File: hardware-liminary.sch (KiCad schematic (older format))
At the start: 2 parts, among them J1 Conn_01x05, J2 Conn_01x05

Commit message: Agregado modulo HLW8032
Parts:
- removed J1, J2: Conn_01x05, Connector_PinHeader_2.54mm:PinHeader_1x05_P2.54mm_Vertical, symbol Connector_Generic:Conn_01x05
- added JB1, JB2, JT1, JT2: Conn_01x03, Connector_PinHeader_2.54mm:PinHeader_1x03_P2.54mm_Vertical, symbol Connector_Generic:Conn_01x03
- added JB3, JT3: Conn_01x05, Connector_PinHeader_2.54mm:PinHeader_1x05_P2.54mm_Vertical, symbol Connector_Generic:Conn_01x05
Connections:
- net Bottom Board/3.3v: now also JB2.1 (Pin_1)
- net Bottom Board/GND: now also JB1.3 (Pin_3)
- net Bottom Board/OpenC: now also JB1.1 (Pin_1)
- net Bottom Board/PIR: now also JB2.3 (Pin_3)
- net Bottom Board/Relay: now also JB3.1 (Pin_1)
- net Top Board/3.3v: now also JT2.1 (Pin_1)
- net Top Board/GND: now also JT1.3 (Pin_3)
- net Top Board/OpenC: now also JT1.1 (Pin_1)
- net Top Board/PIR: now also JT2.3 (Pin_3)
- net Top Board/Relay: now also JT3.1 (Pin_1)
- new net Bottom Board/Enery_Pulses: JB3.5 (Pin_5)
- new net Bottom Board/Enery_Tx: JB3.3 (Pin_3)
- new net Top Board/Enery_Pulses: JT3.5 (Pin_5)
- new net Top Board/Enery_Tx: JT3.3 (Pin_3)
- no-connect marks 0 -> 8
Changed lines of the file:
@@
 $EndDescr
 $Sheet
-S 5550 3150 900  950
+S 5250 3000 900  1300
 U 5F84ED08
 F0 "Top Board" 50
 F1 "top_board.sch" 50
-F2 "3.3v" I L 5550 3300 50
-F3 "GND" U L 5550 3450 50
-F4 "OpenC" O L 5550 3750 50
-F5 "PIR" I L 5550 3600 50
-F6 "Relay" O L 5550 3900 50
+F2 "3.3v" I L 5250 3450 50
+F3 "GND" U L 5250 3300 50
+F4 "OpenC" O L 5250 3150 50
+F5 "PIR" I L 5250 3600 50
+F6 "Relay" O L 5250 3750 50
+F7 "Enery_Tx" I L 5250 3900 50
+F8 "Enery_Pulses" I L 5250 4050 50
 $EndSheet
 $Sheet
-S 2350 3150 1000 950
+S 2200 3000 1000 1300
 U 5F91F411
 F0 "Bottom Board" 50
 F1 "bottom_board.sch" 50
-F2 "3.3v" O R 3350 3300 50
-F3 "GND" U R 3350 3450 50
-F4 "OpenC" I R 3350 3750 50
-F5 "PIR" O R 3350 3600 50
-F6 "Relay" I R 3350 3900 50
+F2 "3.3v" O R 3200 3450 50
+F3 "GND" U R 3200 3300 50
+F4 "OpenC" I R 3200 3150 50
+F5 "PIR" O R 3200 3600 50
+F6 "Relay" I R 3200 3750 50
+F7 "Enery_Tx" O R 3200 3900 50
+F8 "Enery_Pulses" O R 3200 4050 50
 $EndSheet
 $Comp
-L Connector_Generic:Conn_01x05 J1
-U 1 1 5F94C7D4
-P 3850 3600
-F 0 "J1" H 3930 3642 50  0000 L CNN
-F 1 "Conn_01x05" H 3930 3551 50  0000 L CNN
-F 2 "Connector_PinHeader_2.54mm:PinHeader_1x05_P2.54mm_Vertical" H 3850 3600 50  0001 C CNN
-F 3 "~" H 3850 3600 50  0001 C CNN
-	1    3850 3600
+L Connector_Generic:Conn_01x03 JB1
+U 1 1 5F8428AB
+P 3700 3100
+F 0 "JB1" H 3780 3142 50  0000 L CNN
+F 1 "Conn_01x03" H 3780 3051 50  0000 L CNN
+F 2 "Connector_PinHeader_2.54mm:PinHeader_1x03_P2.54mm_Vertical" H 3700 3100 50  0001 C CNN
+F 3 "~" H 3700 3100 50  0001 C CNN
+	1    3700 3100
 	1    0    0    -1
 $EndComp
 $Comp
-L Connector_Generic:Conn_01x05 J2
-U 1 1 5F94DC5D
-P 4800 3600
-F 0 "J2" H 4718 4017 50  0000 C CNN
-F 1 "Conn_01x05" H 4718 3926 50  0000 C CNN
-F 2 "Connector_PinHeader_2.54mm:PinHeader_1x05_P2.54mm_Vertical" H 4800 3600 50  0001 C CNN
-F 3 "~" H 4800 3600 50  0001 C CNN
-	1    4800 3600
+L Connector_Generic:Conn_01x03 JT1
+U 1 1 5F844220
+P 4650 3100
+F 0 "JT1" H 4900 3250 50  0000 C CNN
+F 1 "Conn_01x03" H 4950 3150 50  0000 C CNN
+F 2 "Connector_PinHeader_2.54mm:PinHeader_1x03_P2.54mm_Vertical" H 4650 3100 50  0001 C CNN
+F 3 "~" H 4650 3100 50  0001 C CNN
+	1    4650 3100
+	-1   0    0    -1
+$EndComp
+NoConn ~ 3500 3100
+NoConn ~ 4850 3100
+Wire Wire Line
+	3200 3150 3300 3150
+Wire Wire Line
+	3300 3150 3300 3000
+Wire Wire Line
+	3300 3000 3500 3000
+Wire Wire Line
+	3200 3300 3350 3300
+Wire Wire Line
+	3350 3300 3350 3200
+Wire Wire Line
+	3350 3200 3500 3200
+Wire Wire Line
+	5250 3300 5050 3300
+Wire Wire Line
+	5050 3300 5050 3200
+Wire Wire Line
+	5050 3200 4850 3200
+Wire Wire Line
+	5250 3150 5150 3150
+Wire Wire Line
+	5150 3150 5150 3000
+Wire Wire Line
+	5150 3000 4850 3000
+$Comp
+L Connector_Generic:Conn_01x03 JB2
+U 1 1 5F84642D
+P 3700 3500
+F 0 "JB2" H 3780 3542 50  0000 L CNN
+F 1 "Conn_01x03" H 3780 3451 50  0000 L CNN
+F 2 "Connector_PinHeader_2.54mm:PinHeader_1x03_P2.54mm_Vertical" H 3700 3500 50  0001 C CNN
+F 3 "~" H 3700 3500 50  0001 C CNN
+	1    3700 3500
+	1    0    0    -1
+$EndComp
+$Comp
+L Connector_Generic:Conn_01x03 JT2
+U 1 1 5F846D28
+P 4650 3500
+F 0 "JT2" H 4900 3700 50  0000 C CNN
+F 1 "Conn_01x03" H 4950 3600 50  0000 C CNN
+F 2 "Connector_PinHeader_2.54mm:PinHeader_1x03_P2.54mm_Vertical" H 4650 3500 50  0001 C CNN
+F 3 "~" H 4650 3500 50  0001 C CNN
+	1    4650 3500
 	-1   0    0    -1
 $EndComp
 Wire Wire Line
-	3350 3300 3650 3300
+	3200 3600 3500 3600
 Wire Wire Line
-	3650 3300 3650 3400
+	3200 3450 3350 3450
 Wire Wire Line
-	3350 3450 3500 3450
+	3350 3450 3350 3400
 Wire Wire Line
-	3500 3450 3500 3500
+	3350 3400 3500 3400
 Wire Wire Line
-	3500 3500 3650 3500
+	4850 3600 5250 3600
 Wire Wire Line
-	3350 3600 3650 3600
+	5250 3450 5100 3450
 Wire Wire Line
-	3350 3750 3500 3750
+	5100 3450 5100 3400
 Wire Wire Line
-	3500 3750 3500 3700
+	5100 3400 4850 3400
+NoConn ~ 4850 3500
+NoConn ~ 3500 3500
+$Comp
+L Connector_Generic:Conn_01x05 JB3
+U 1 1 5F84843D
+P 3700 3950
+F 0 "JB3" H 3780 3992 50  0000 L CNN
+F 1 "Conn_01x05" H 3780 3901 50  0000 L CNN
+F 2 "Connector_PinHeader_2.54mm:PinHeader_1x05_P2.54mm_Vertical" H 3700 3950 50  0001 C CNN
+F 3 "~" H 3700 3950 50  0001 C CNN
+	1    3700 3950
+	1    0    0    -1
+$EndComp
+$Comp
+L Connector_Generic:Conn_01x05 JT3
+U 1 1 5F84914E
+P 4650 3950
+F 0 "JT3" H 4900 4150 50  0000 C CNN
+F 1 "Conn_01x05" H 4950 4050 50  0000 C CNN
+F 2 "Connector_PinHeader_2.54mm:PinHeader_1x05_P2.54mm_Vertical" H 4650 3950 50  0001 C CNN
+F 3 "~" H 4650 3950 50  0001 C CNN
+	1    4650 3950
+	-1   0    0    -1
+$EndComp
 Wire Wire Line
-	3500 3700 3650 3700
+	3200 3750 3500 3750
 Wire Wire Line
-	3350 3900 3650 3900
+	3200 3900 3350 3900
 Wire Wire Line
-	3650 3900 3650 3800
+	3350 3900 3350 3950
 Wire Wire Line
-	5000 3600 5550 3600
+	3350 3950 3500 3950
 Wire Wire Line
-	5000 3500 5300 3500
+	3200 4050 3300 4050
 Wire Wire Line
-	5300 3500 5300 3450
+	3300 4050 3300 4150
 Wire Wire Line
-	5300 3450 5550 3450
+	3300 4150 3500 4150
 Wire Wire Line
-	5000 3800 5000 3900
+	5250 3750 4850 3750
 Wire Wire Line
-	5000 3900 5550 3900
+	5250 3900 5050 3900
 Wire Wire Line
-	5550 3750 5300 3750
+	5050 3900 5050 3950
 Wire Wire Line
-	5300 3750 5300 3700
+	5050 3950 4850 3950
 Wire Wire Line
-	5300 3700 5000 3700
+	5250 4050 5150 4050
 Wire Wire Line
-	5000 3400 5150 3400
+	5150 4050 5150 4150
 Wire Wire Line
-	5150 3400 5150 3300
-Wire Wire Line
-	5150 3300 5550 3300
+	5150 4150 4850 4150
+NoConn ~ 3500 3850
+NoConn ~ 3500 4050
+NoConn ~ 4850 3850
+NoConn ~ 4850 4050
 $EndSCHEMATC

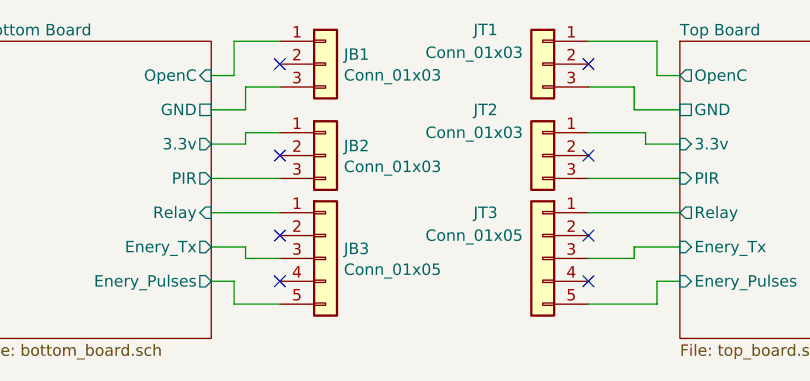
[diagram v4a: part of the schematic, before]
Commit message: Esquematico reordenado
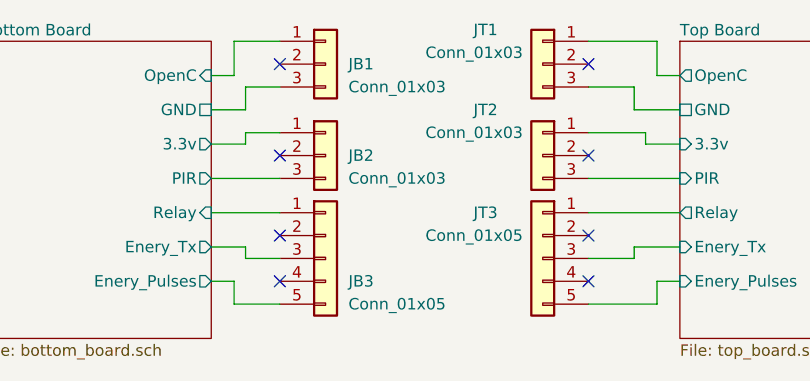
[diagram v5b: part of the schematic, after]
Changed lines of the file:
@@
 U 1 1 5F8428AB
 P 3700 3100
-F 0 "JB1" H 3780 3142 50  0000 L CNN
-F 1 "Conn_01x03" H 3780 3051 50  0000 L CNN
+F 0 "JB1" H 3800 3100 50  0000 L CNN
+F 1 "Conn_01x03" H 3800 3000 50  0000 L CNN
 F 2 "Connector_PinHeader_2.54mm:PinHeader_1x03_P2.54mm_Vertical" H 3700 3100 50  0001 C CNN
 F 3 "~" H 3700 3100 50  0001 C CNN
@@
 U 1 1 5F84642D
 P 3700 3500
-F 0 "JB2" H 3780 3542 50  0000 L CNN
-F 1 "Conn_01x03" H 3780 3451 50  0000 L CNN
+F 0 "JB2" H 3800 3500 50  0000 L CNN
+F 1 "Conn_01x03" H 3800 3400 50  0000 L CNN
 F 2 "Connector_PinHeader_2.54mm:PinHeader_1x03_P2.54mm_Vertical" H 3700 3500 50  0001 C CNN
 F 3 "~" H 3700 3500 50  0001 C CNN
@@
 U 1 1 5F84843D
 P 3700 3950
-F 0 "JB3" H 3780 3992 50  0000 L CNN
-F 1 "Conn_01x05" H 3780 3901 50  0000 L CNN
+F 0 "JB3" H 3800 3850 50  0000 L CNN
+F 1 "Conn_01x05" H 3800 3750 50  0000 L CNN
 F 2 "Connector_PinHeader_2.54mm:PinHeader_1x05_P2.54mm_Vertical" H 3700 3950 50  0001 C CNN
 F 3 "~" H 3700 3950 50  0001 C CNN
